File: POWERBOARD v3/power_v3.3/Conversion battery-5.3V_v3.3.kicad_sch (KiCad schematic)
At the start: 14 parts, among them U3 TPS62160DSG

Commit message: added footprints
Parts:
- removed 5.3V2, GND2: Conn_01x02, Connector_PinHeader_2.00mm:PinHeader_1x02_P2.00mm_Vertical, symbol Connector_Generic:Conn_01x02
- added BUCK5V3, GND2: TestPoint, TestPoint:TestPoint_Keystone_5000-5004_Miniature, symbol Connector:TestPoint
- Cout1: footprint Capacitor_SMD:C_1210_3225Metric -> Capacitor_SMD:C_1206_3216Metric
- L2: footprint Inductor_SMD:L_Bourns-SRN4018 -> 78438336022:78438336022
- R10, R11, R12: footprint Resistor_SMD:R_0805_2012Metric -> Resistor_SMD:R_0603_1608Metric
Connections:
- net GND: now also GND2.1
- net output_at_5.3: now also BUCK5V3.1

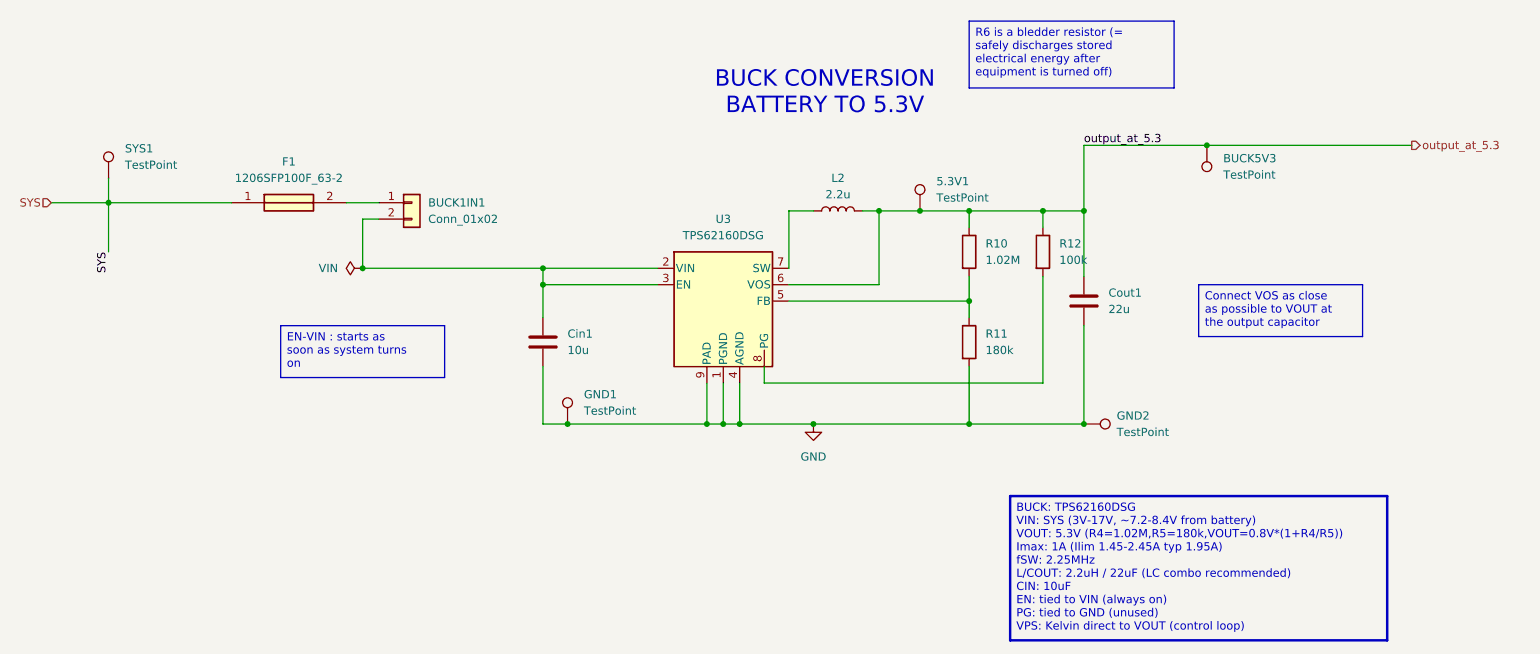
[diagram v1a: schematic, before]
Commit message: finished footprint assignment, added on-off general switch
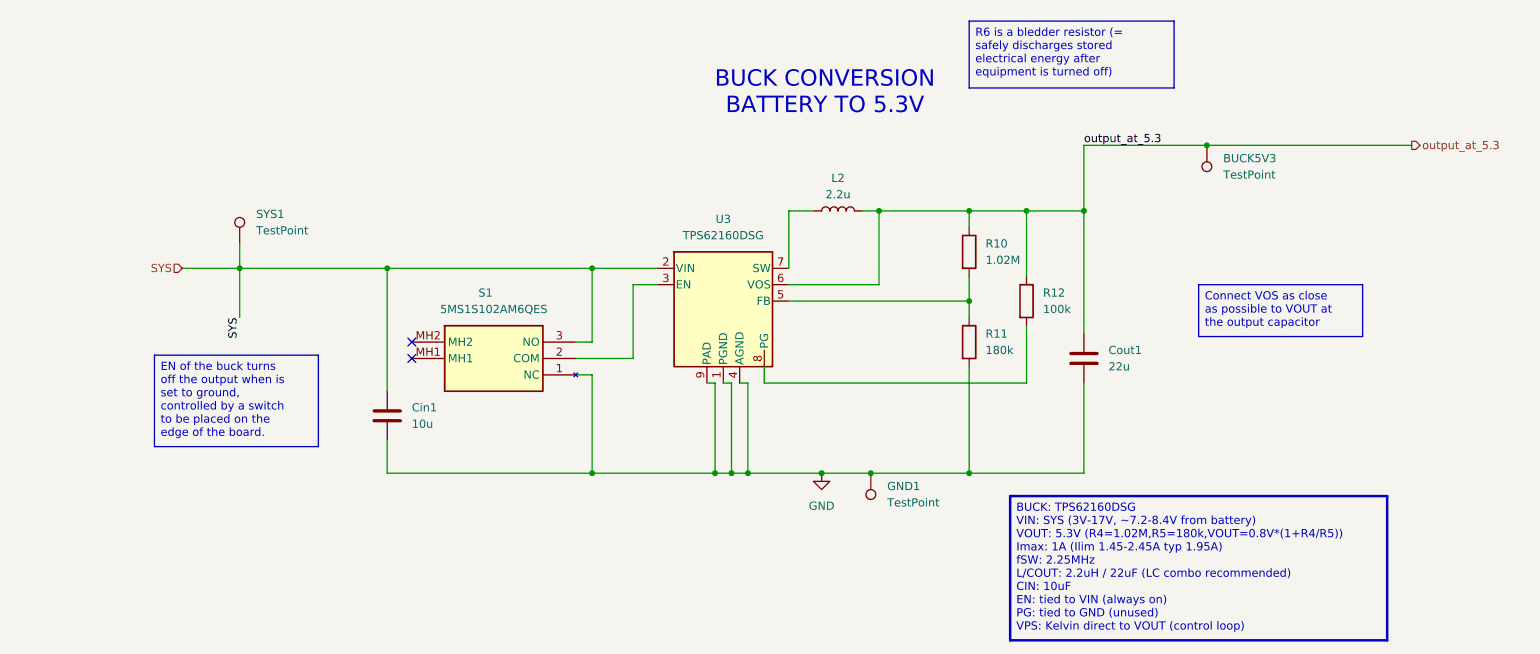
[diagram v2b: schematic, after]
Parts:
- removed 5.3V1, GND2: TestPoint, TestPoint:TestPoint_Keystone_5000-5004_Miniature, symbol Connector:TestPoint
- removed BUCK1IN1: Conn_01x02, Connector_PinHeader_2.00mm:PinHeader_1x02_P2.00mm_Vertical, symbol Connector_Generic:Conn_01x02
- removed F1: 1206SFP100F_63-2, Fuse:Fuse_1206_3216Metric, symbol 1206SFP100F_63-2:1206SFP100F_63-2
- added S1: 5MS1S102AM6QES, switchonoff:5MS1S102AM6QES, symbol 5MS1S102AM6QES:5MS1S102AM6QES
- U3: footprint Package_SON:WSON-8-1EP_2x2mm_P0.5mm_EP0.9x1.6mm_ThermalVias -> TPS62160DSGT:SON50P200X200X80-9N
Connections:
- net GND: now also S1.1 (NC)
- net SYS: now also Cin1.1, U3.2 (VIN), S1.3 (NO)
- new net: S1.2 (COM), U3.3 (EN)
- no-connect marks 0 -> 2
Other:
- moved on the sheet: Cin1, Cout1, GND1, R12, SYS1

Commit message: (nearly) finished schematic and layout, beginning routing (hooooooly)
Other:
- moved on the sheet: BUCK5V3, Cin1, Cout1, GND1, L2, R10, R11, R12, S1, SYS1, U3
